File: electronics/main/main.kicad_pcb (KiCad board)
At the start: 2 copper layers, 116 parts, among them IC1 ATMEGA8-P, J1 CABLE, J2 CABLE, J3 CABLE, J4 CABLE, J5 CABLE, J6 CABLE, J7 CABLE, J8 CABLE, P1 5v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

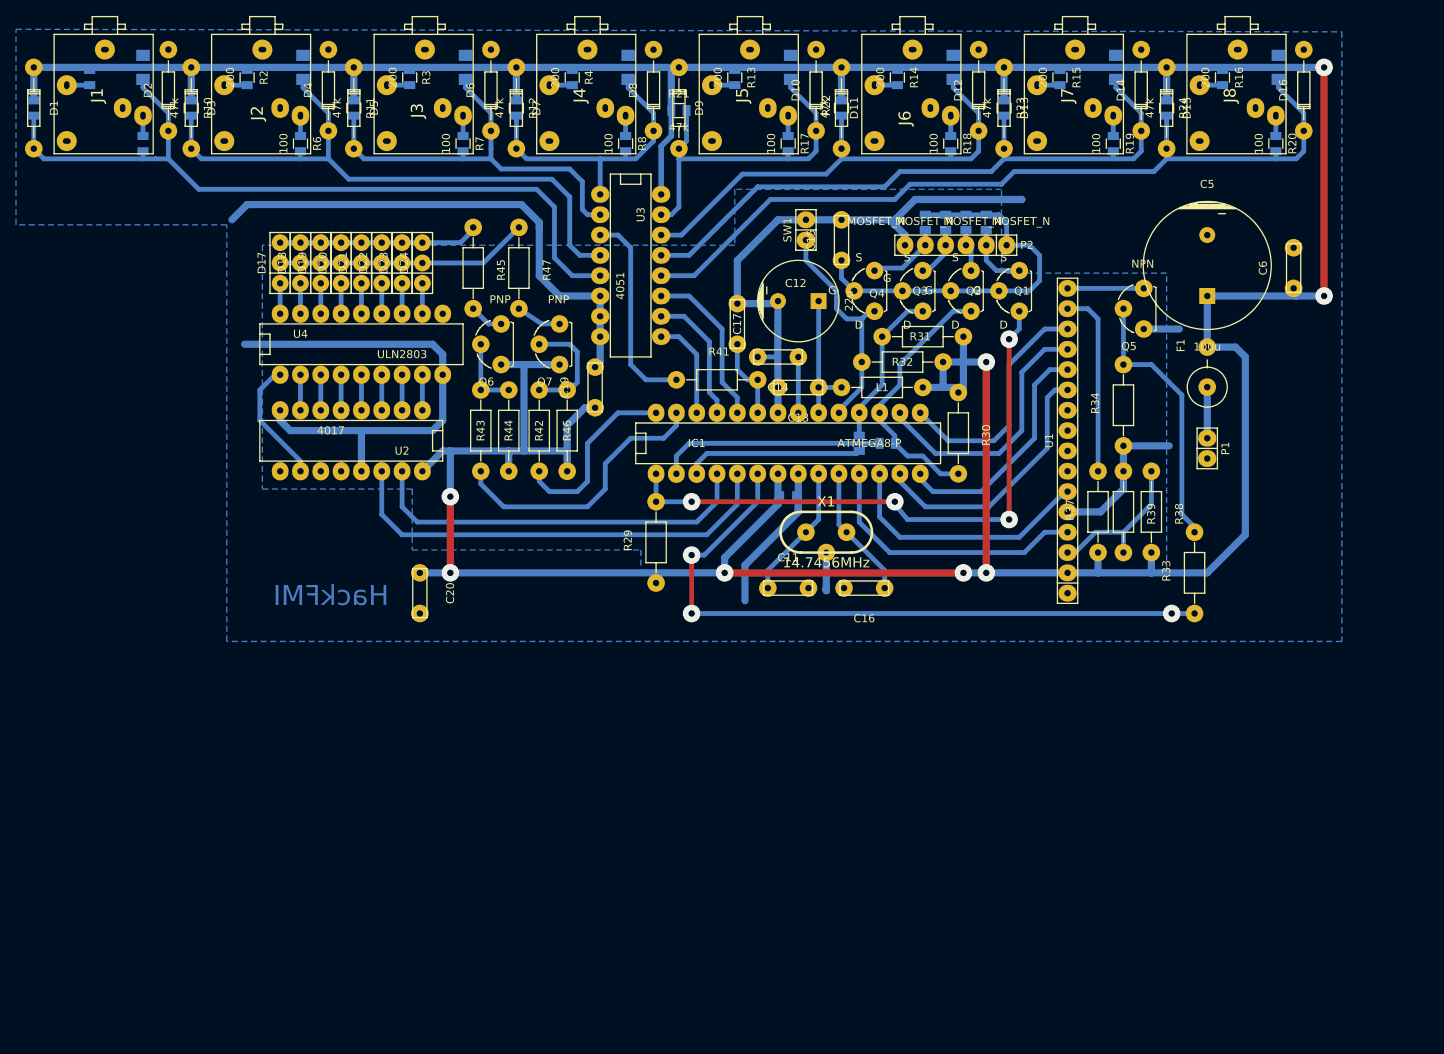
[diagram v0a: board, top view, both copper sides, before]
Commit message: add mounting holes
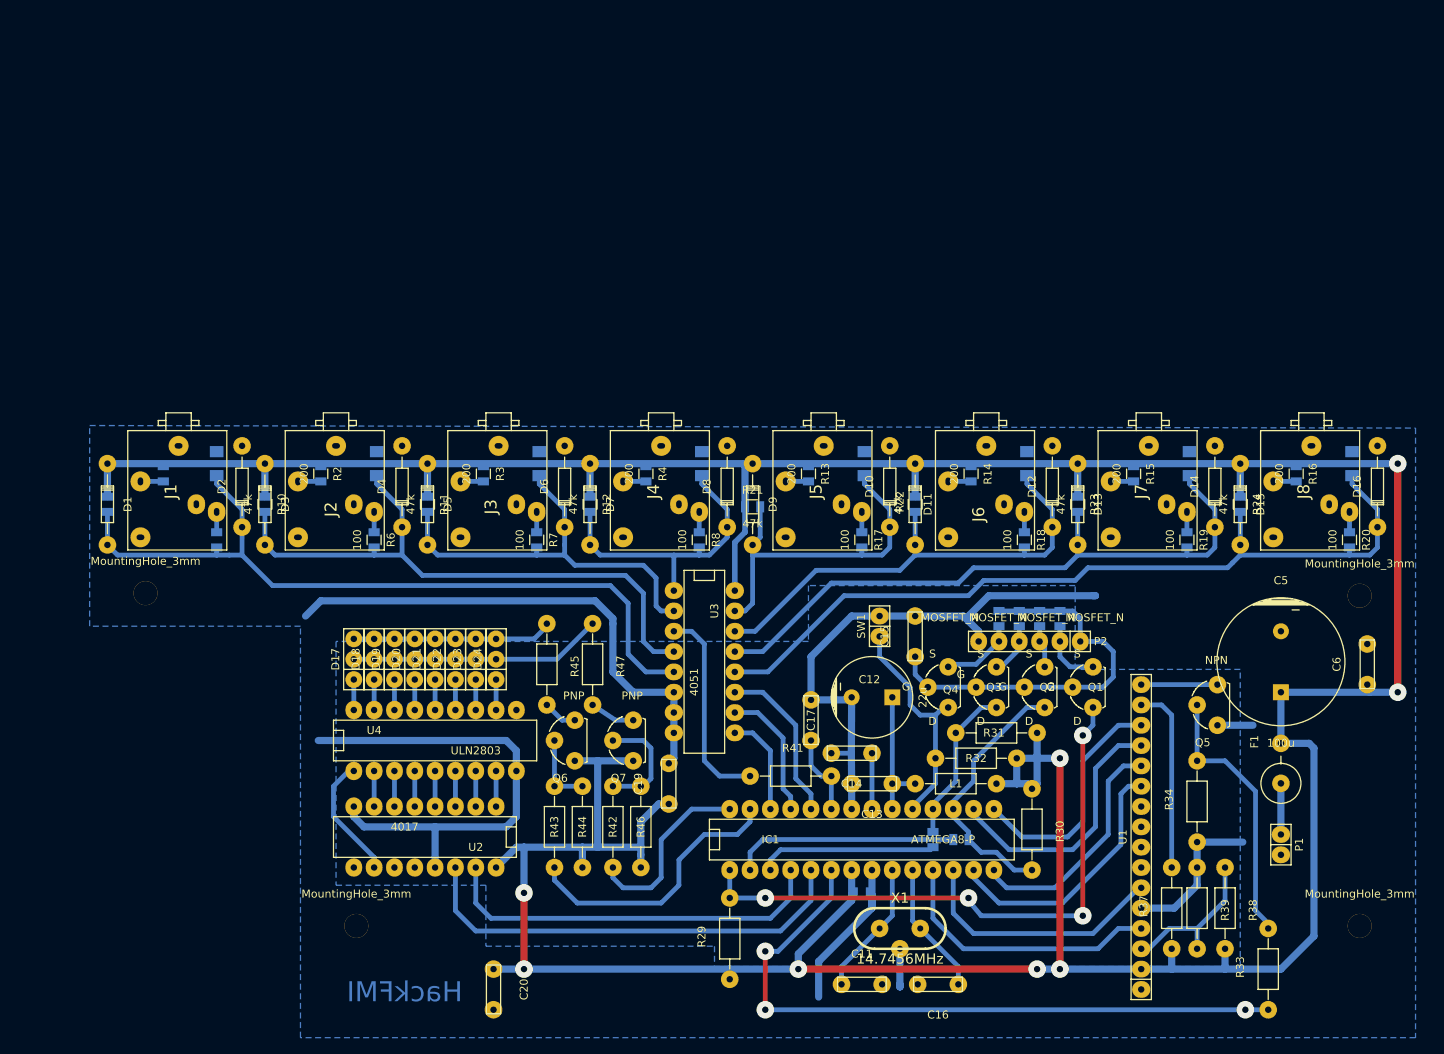
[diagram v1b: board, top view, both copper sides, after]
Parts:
- added MountingHole_3mm: VAL**, Mounting_Holes:MountingHole_3mm, F.Cu at (225.7, 85.7)
- added MountingHole_3mm: VAL**, Mounting_Holes:MountingHole_3mm, F.Cu at (74.0, 85.4)
- added MountingHole_3mm: VAL**, Mounting_Holes:MountingHole_3mm, F.Cu at (100.3, 127.0)
- added MountingHole_3mm: VAL**, Mounting_Holes:MountingHole_3mm, F.Cu at (225.7, 127.0)
- moved C11 50.4 mm to (163.5, 134.3)
- moved C15 50.4 mm to (170.2, 90.8)
- moved C16 50.4 mm to (173.0, 134.3)
- moved F1 50.4 mm to (215.9, 106.7)
- moved Q6 50.4 mm to (127.6, 103.8)
- moved C1 50.4 mm to (82.9, 69.2)
- moved C13 50.4 mm to (164.8, 109.2)
- moved C2 50.4 mm to (102.9, 69.2)
- moved C5 50.4 mm to (215.9, 94.0)
- moved C7 50.4 mm to (163.8, 69.2)
- moved C8 50.4 mm to (184.2, 69.2)
- moved C9 50.4 mm to (204.5, 69.2)
- moved D1 50.4 mm to (69.2, 74.3)
- moved D11 50.4 mm to (170.2, 74.3)
- moved D13 50.4 mm to (190.5, 74.3)
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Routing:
- net VCC: track 530.0 -> 529.5 mm
